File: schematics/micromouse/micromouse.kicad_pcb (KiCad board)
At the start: 4 copper layers, 70 x 90 mm, 64 parts, among them J1 TOF_LEFT, J10 MotorB_Conn, J11 BMI_ConnB, J12 BMI_ConnA, J13 StepDown_{In+}, J14 StepDown_{In-}, J15 StepDown_{Out+}, J16 StepDown_{Out-}, J2 TOF_FRONTLEFT, J3 TOF_FRONTRIGHT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

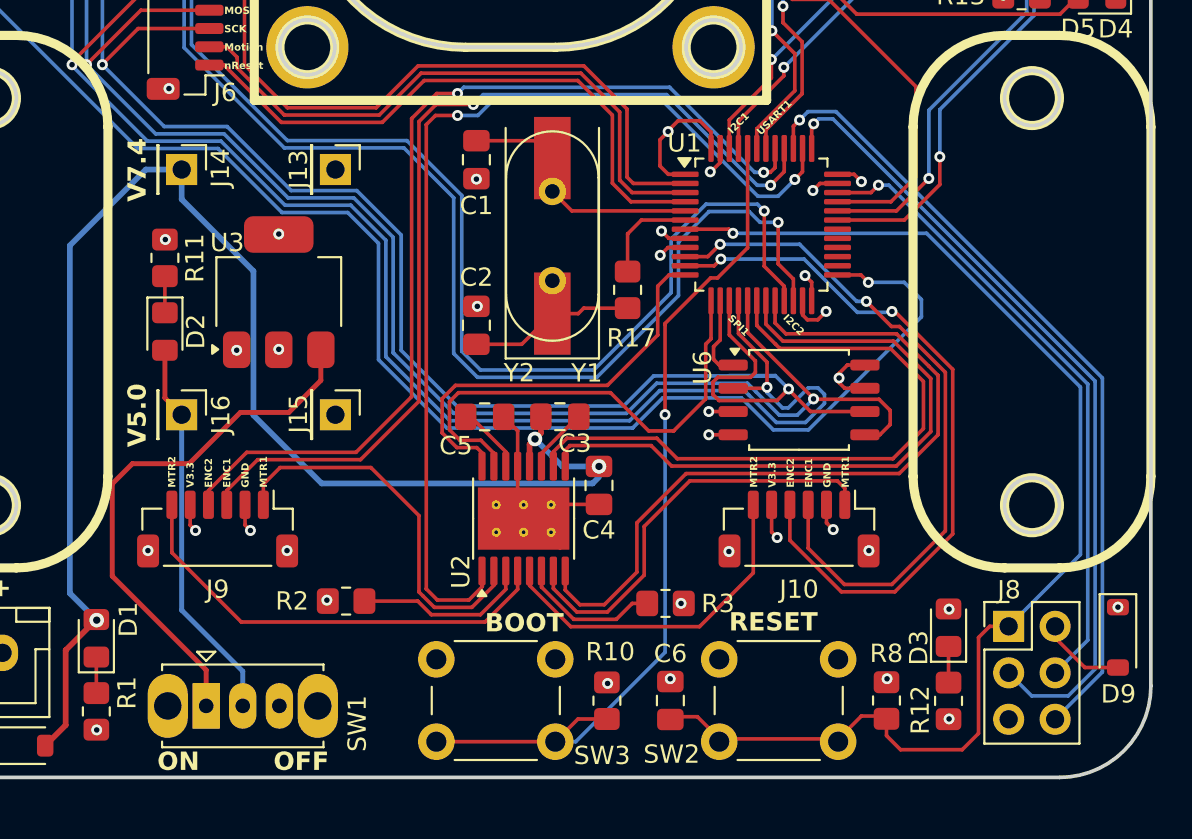
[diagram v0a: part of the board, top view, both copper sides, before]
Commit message: Schematic: * Add microSD card socket
PCB:
* Change BOOT and RESET buttons
* Add and connect microSD card socket
* Fix some CRC errors
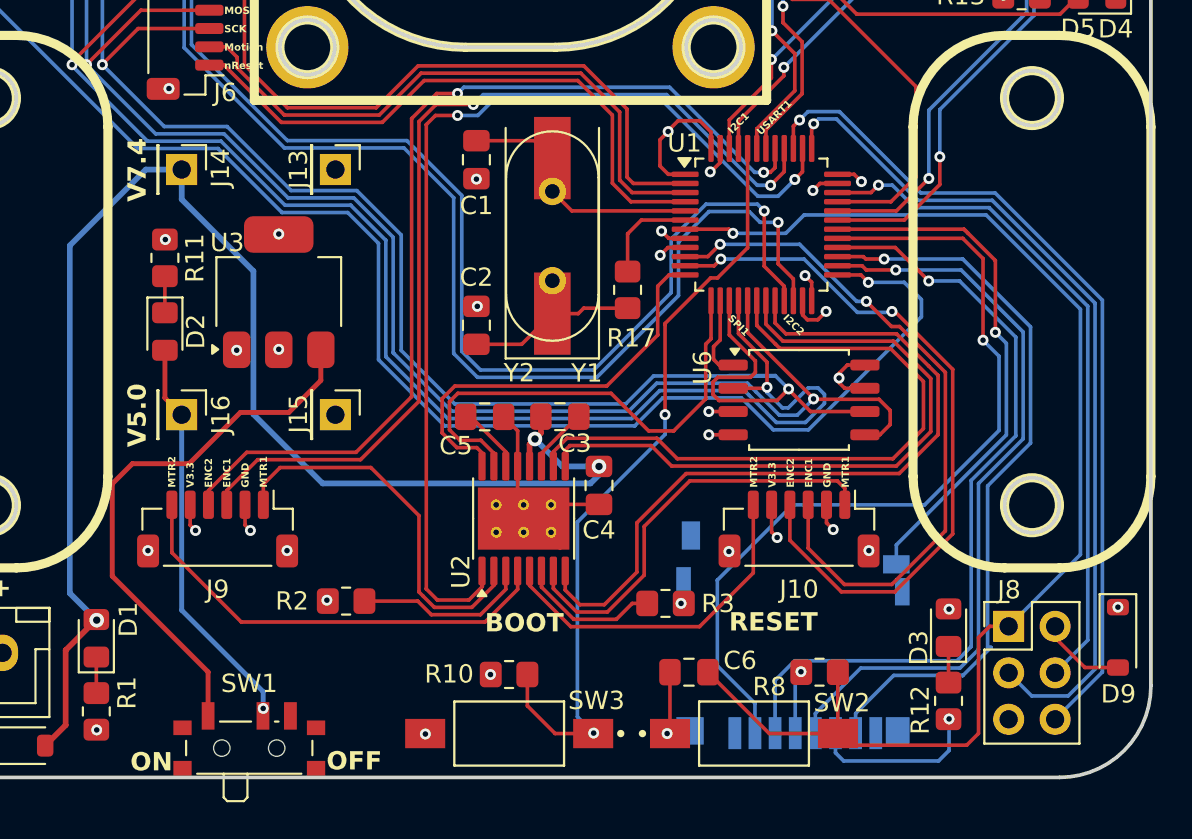
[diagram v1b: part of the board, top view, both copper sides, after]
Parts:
- added J18: Micro_SD_Card_Det1, Connector_Card:microSD_HC_Hirose_DM3D-SF, B.Cu at (155.8, 105.6)
- SW1: footprint Button_Switch_THT:SW_Slide_SPDT_Straight_CK_OS102011MS2Q -> Button_Switch_SMD:SW_SPDT_PCM12
- SW2, SW3: footprint Button_Switch_THT:SW_PUSH_6mm_H5mm -> FSMSM:TE_FSMSM
- moved R10 5.53 mm to (140.3, 107.8), turned to 0 degrees
- moved SW2 4.48 mm to (153.7, 111.0)
- moved R8 3.97 mm to (157.3, 107.6), turned to 180 degrees
- moved SW1 3.07 mm to (126.1, 111.5)
- moved SW3 2.56 mm to (140.3, 111.0)
- moved C6 1.85 mm to (150.2, 107.6), turned to 180 degrees
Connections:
- U1 pad 26: unconnected-(U1-PB13-Pad26) -> /SPI2_{clk}
- U1 pad 27: unconnected-(U1-PB14-Pad27) -> /SPI2_{miso}
- U1 pad 28: unconnected-(U1-PB15-Pad28) -> /SPI2_{mosi}
- U1 pad 29: unconnected-(U1-PA8-Pad29) -> /SD_{cs}
- U1 pad 30: unconnected-(U1-PA9-Pad30) -> /SD_{detect}
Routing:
- net /SD_{cs}: track 0.00 -> 46.2 mm, vias 0 -> 1
- net /SPI2_{mosi}: track 0.00 -> 44.1 mm, vias 0 -> 1
- net /SPI2_{clk}: track 0.00 -> 41.4 mm, vias 0 -> 1
- net /SPI2_{miso}: track 0.00 -> 40.8 mm, vias 0 -> 1
- net /SD_{detect}: track 0.00 -> 29.0 mm, vias 0 -> 1
- net GND: track 32.2 -> 45.6 mm
- net /BOOT: track 47.5 -> 42.4 mm, vias 1 -> 2
- net /RESET: track 66.5 -> 70.4 mm
- net VCC_{3.3}: track 26.6 -> 30.1 mm, vias 21 -> 22
- net /SWo: track 44.2 -> 46.7 mm
- net /SW_{dio}: track 35.6 -> 38.0 mm
- net /SW_{clk}: track 44.4 -> 46.9 mm
- net Net-(U1-PD0): track 12.2 -> 14.1 mm
- net Net-(C2-Pad1): track 9.08 -> 10.9 mm
- net Net-(SW1-A): track 29.7 -> 30.3 mm
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
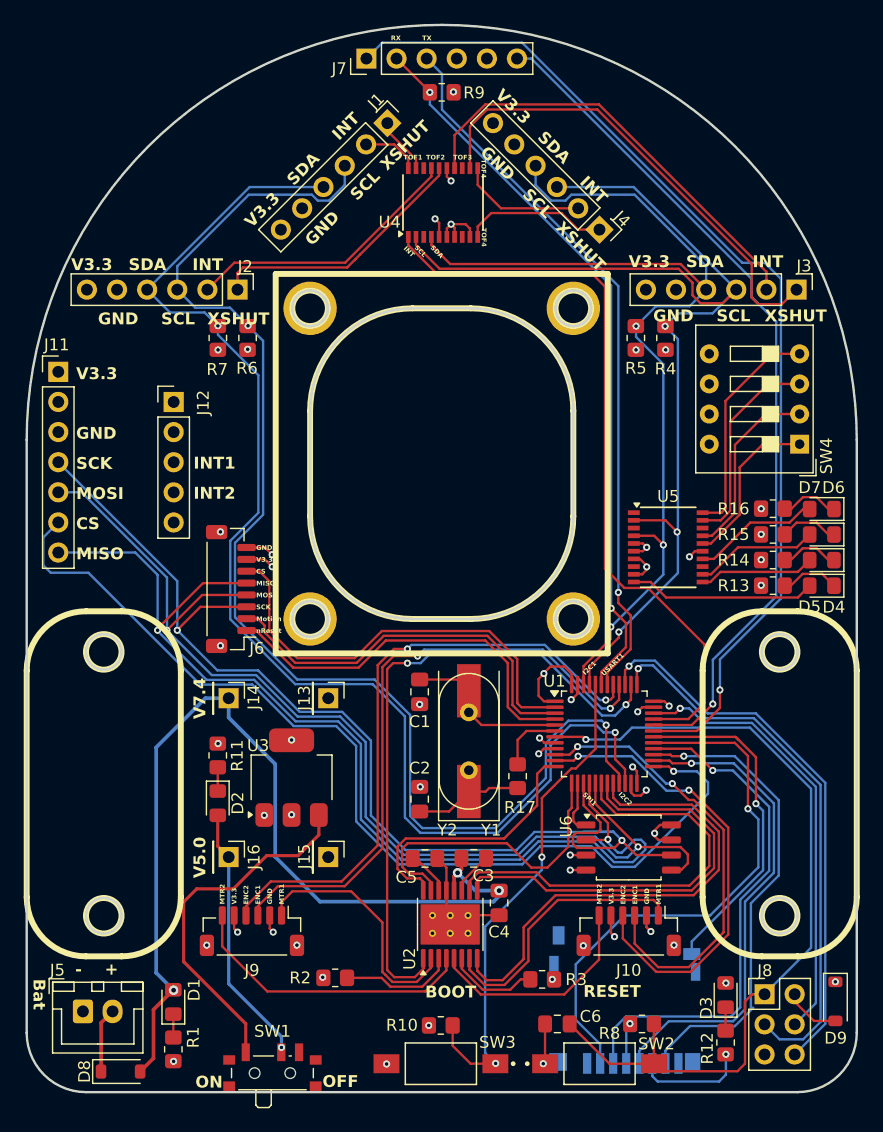
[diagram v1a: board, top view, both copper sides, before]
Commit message: Solve DRC errors
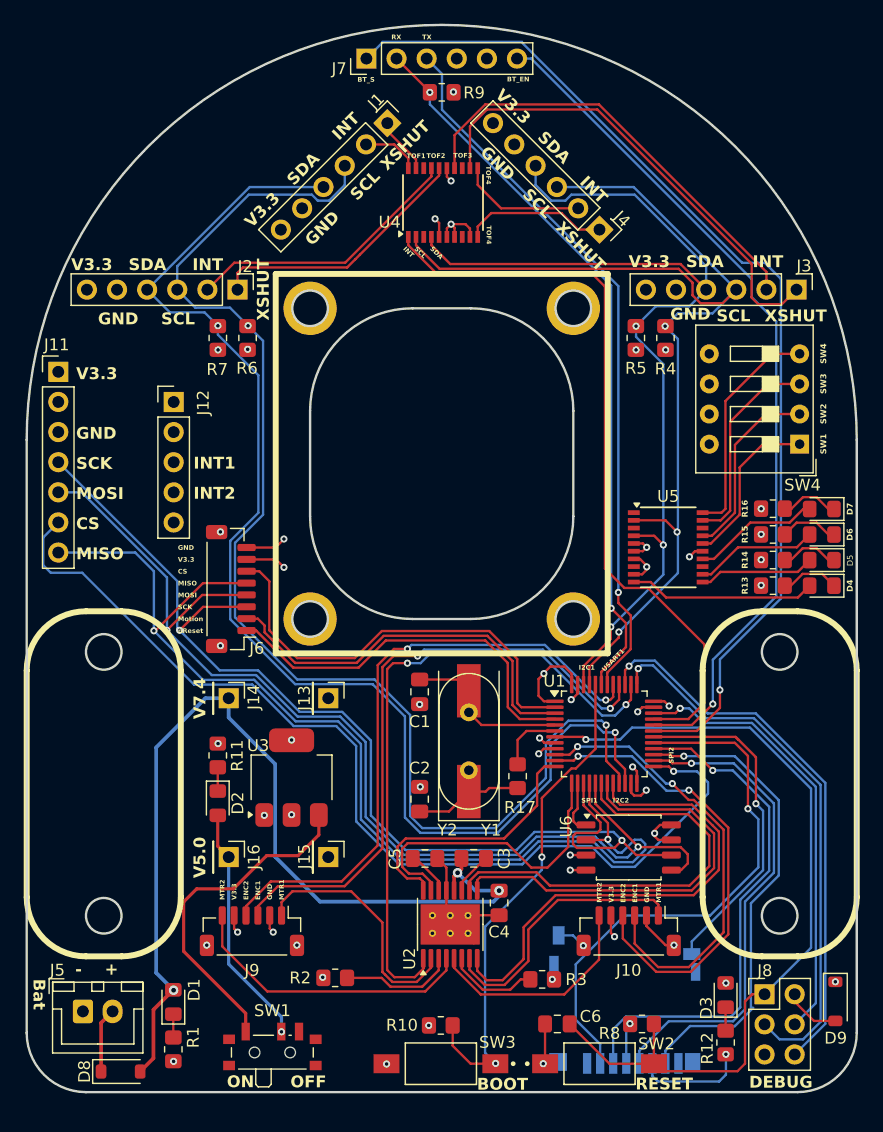
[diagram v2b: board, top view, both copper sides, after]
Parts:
- moved SW1 1.74 mm to (126.1, 109.7)
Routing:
- net GND: track 45.6 -> 51.4 mm, vias 32 -> 31
- net /SPI1_{clk}: track 94.6 -> 91.7 mm
- net Net-(SW1-A): track 30.3 -> 28.5 mm
- net VCC_{5}: track 22.0 -> 20.5 mm
- net VCC_{3.3}: track 30.1 -> 31.1 mm
- net /BT_{enable}: track 72.9 -> 72.1 mm
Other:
- board text added: "BT_EN"
- board text added: "BT_S"
- board text added: "DEBUG"
- board text added: "SPI2"
- board text added: "SW1"
- board text added: "SW2"
- board text added: "SW3"
- board text added: "SW4"

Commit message: Add QR to tag "MousePCB/1.0"
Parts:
- added G***: LOGO, QR:QR_MousePCB_1.0, B.Cu at (155.7, 87.7)
- added REF**: OSHW-Symbol_6.7x6mm_SilkScreen, Symbol:OSHW-Symbol_6.7x6mm_SilkScreen, B.Cu at (113.6, 90.4)
- added REF**: KiCad-Logo2_5mm_SilkScreen, Symbol:KiCad-Logo2_5mm_SilkScreen, B.Cu at (113.6, 83.1)
